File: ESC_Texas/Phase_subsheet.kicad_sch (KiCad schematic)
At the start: 14 parts, among them IC3 AD8411AWBRZ, IC4 MC78L05ACHT1G, J5 Conn_01x03_Pin, J6 Conn_01x03_Pin

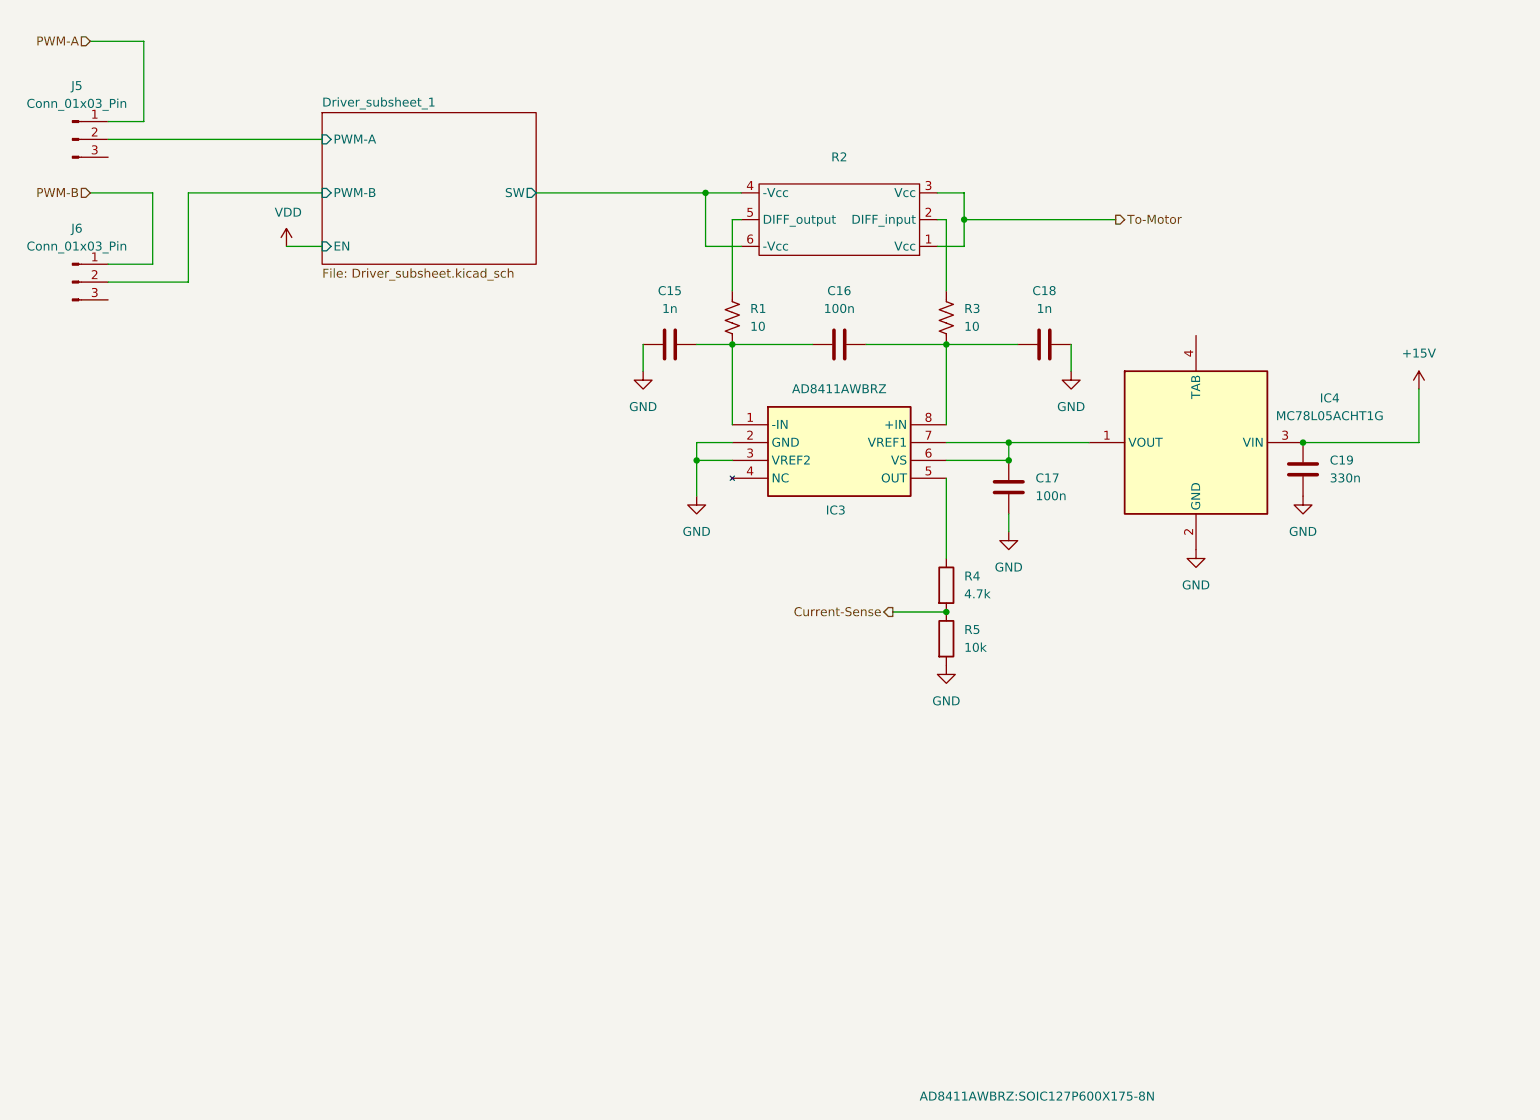
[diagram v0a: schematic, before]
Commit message: Added bypass capacitors to dc/dc...
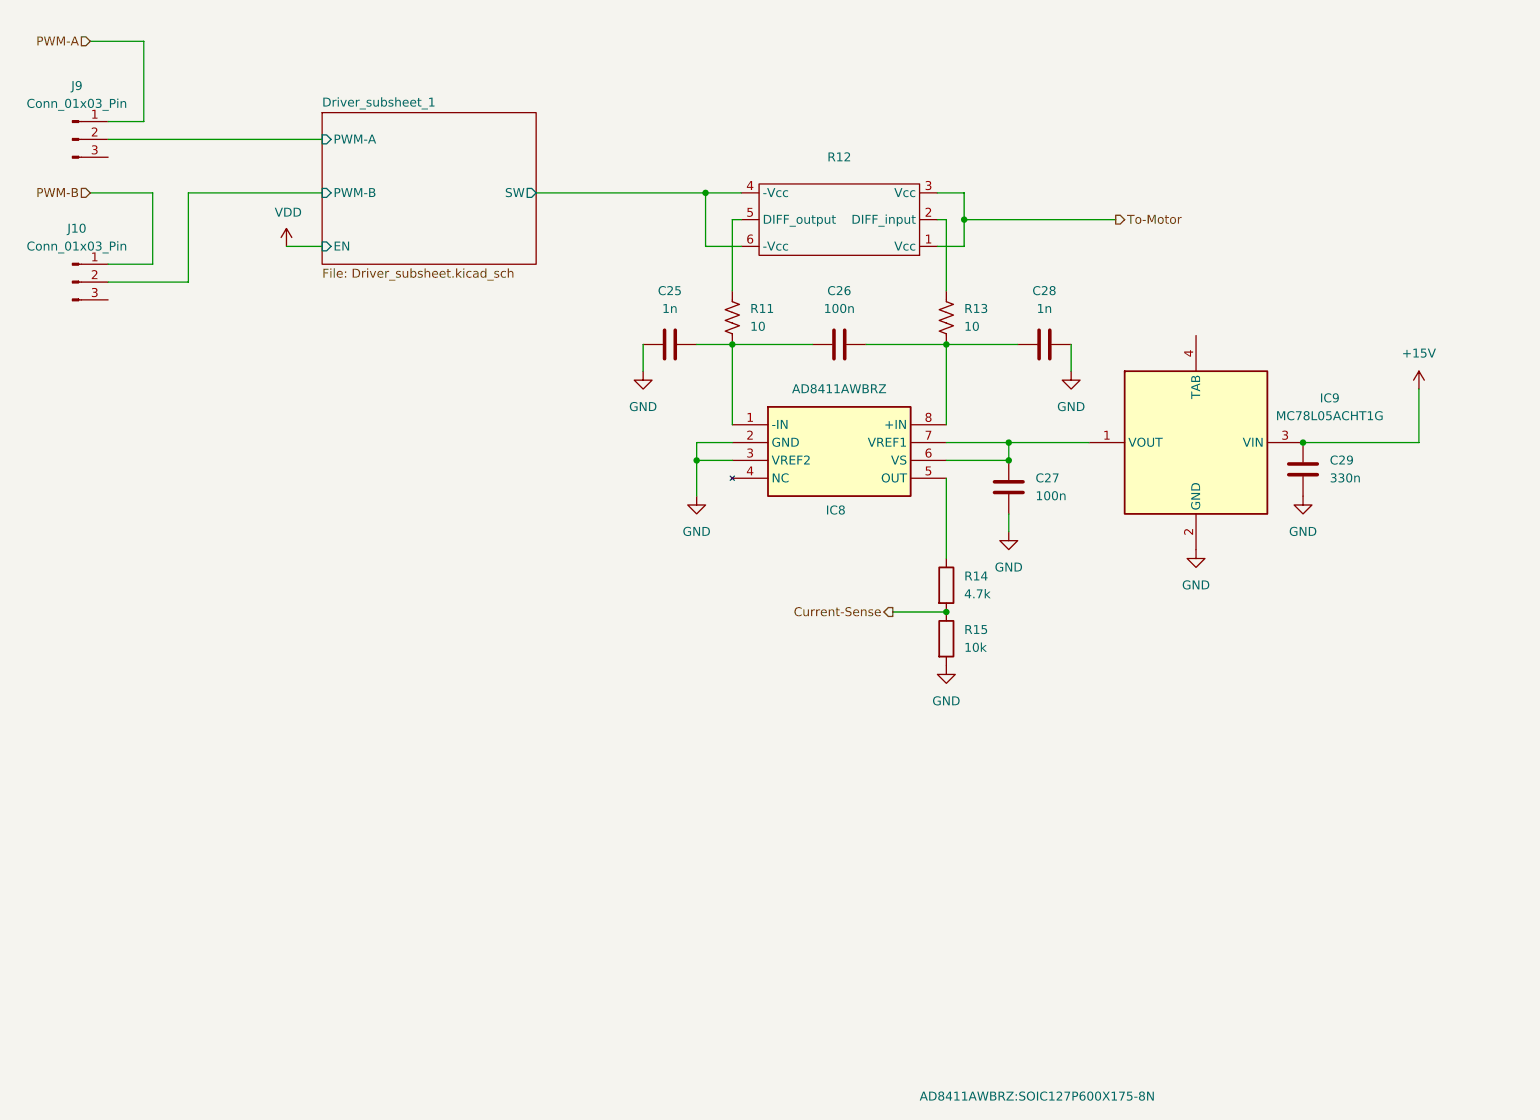
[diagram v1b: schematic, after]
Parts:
- renumbered C15 to C25, C16 to C26, C17 to C27, C18 to C28, C19 to C29, IC3 to IC8, IC4 to IC9, J6 to J10, J5 to J9, R1 to R11, R2 to R12, R3 to R13, R4 to R14, R5 to R15
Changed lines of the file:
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@@
 		(dnp no)
 		(fields_autoplaced yes)
-		(property "Reference" "C15"
+		(property "Reference" "C25"
 			(at 143.51 88.9 90)
 			(effects
@@
 		(dnp no)
 		(fields_autoplaced yes)
-		(property "Reference" "J5"
+		(property "Reference" "J9"
 			(at 59.055 59.69 0)
 			(effects
@@
 		(dnp no)
 		(fields_autoplaced yes)
-		(property "Reference" "#PWR037"
+		(property "Reference" "#PWR065"
 			(at 233.68 124.46 0)
 			(effects
@@
 		(dnp no)
 		(fields_autoplaced yes)
-		(property "Reference" "#PWR031"
+		(property "Reference" "#PWR059"
 			(at 139.7 106.68 0)
 			(effects
@@
 		(dnp no)
 		(fields_autoplaced yes)
-		(property "Reference" "C19"
+		(property "Reference" "C29"
 			(at 237.49 113.0299 0)
 			(effects
@@
 		(dnp no)
 		(fields_autoplaced yes)
-		(property "Reference" "#PWR034"
+		(property "Reference" "#PWR062"
 			(at 191.77 129.54 0)
 			(effects
@@
 		(dnp no)
 		(fields_autoplaced yes)
-		(property "Reference" "C17"
+		(property "Reference" "C27"
 			(at 195.58 115.5699 0)
 			(effects
@@
 		(dnp no)
 		(fields_autoplaced yes)
-		(property "Reference" "J6"
+		(property "Reference" "J10"
 			(at 59.055 80.01 0)
 			(effects
@@
 		(dnp no)
 		(fields_autoplaced yes)
-		(property "Reference" "R4"
+		(property "Reference" "R14"
 			(at 185.42 129.5399 0)
 			(effects
@@
 		(dnp no)
 		(fields_autoplaced yes)
-		(property "Reference" "#PWR033"
+		(property "Reference" "#PWR061"
 			(at 182.88 148.59 0)
 			(effects
@@
 		(on_board yes)
 		(dnp no)
-		(property "Reference" "#PWR030"
+		(property "Reference" "#PWR058"
 			(at 88.9 86.36 0)
 			(effects
@@
 		(dnp no)
 		(fields_autoplaced yes)
-		(property "Reference" "R1"
+		(property "Reference" "R11"
 			(at 154.94 91.4399 0)
 			(effects
@@
 		(dnp no)
 		(fields_autoplaced yes)
-		(property "Reference" "C18"
+		(property "Reference" "C28"
 			(at 196.85 88.9 90)
 			(effects
@@
 		(dnp no)
 		(fields_autoplaced yes)
-		(property "Reference" "C16"
+		(property "Reference" "C26"
 			(at 167.64 88.9 90)
 			(effects
@@
 		(dnp no)
 		(fields_autoplaced yes)
-		(property "Reference" "R2"
+		(property "Reference" "R12"
 			(at 167.64 69.85 0)
 			(effects
@@
 		(dnp no)
 		(fields_autoplaced yes)
-		(property "Reference" "#PWR032"
+		(property "Reference" "#PWR060"
 			(at 147.32 124.46 0)
 			(effects
@@
 		(on_board yes)
 		(dnp no)
-		(property "Reference" "IC3"
+		(property "Reference" "IC8"
 			(at 167.132 120.142 0)
 			(effects
@@
 		(dnp no)
 		(fields_autoplaced yes)
-		(property "Reference" "IC4"
+		(property "Reference" "IC9"
 			(at 237.49 104.1714 0)
 			(effects
@@
 		(dnp no)
 		(fields_autoplaced yes)
-		(property "Reference" "#PWR035"
+		(property "Reference" "#PWR063"
 			(at 200.66 106.68 0)
 			(effects
@@
 		(dnp no)
 		(fields_autoplaced yes)
-		(property "Reference" "#PWR036"
+		(property "Reference" "#PWR064"
 			(at 218.44 132.08 0)
 			(effects
@@
 		(dnp no)
 		(fields_autoplaced yes)
-		(property "Reference" "R5"
+		(property "Reference" "R15"
 			(at 185.42 137.1599 0)
 			(effects
@@
 		(dnp no)
 		(fields_autoplaced yes)
-		(property "Reference" "R3"
+		(property "Reference" "R13"
 			(at 185.42 91.4399 0)
 			(effects
@@
 		(dnp no)
 		(fields_autoplaced yes)
-		(property "Reference" "#PWR038"
+		(property "Reference" "#PWR066"
 			(at 250.19 106.68 0)
 			(effects

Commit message: PCB layout done
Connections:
- net GND: now also IC9.4 (TAB)
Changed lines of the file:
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@@
+	(wire
+		(pts
+			(xy 218.44 91.44) (xy 218.44 95.25)
+		)
+		(stroke
+			(width 0)
+			(type default)
+		)
+	)
 	(wire
 		(pts
@@
 	(wire
 		(pts
+			(xy 224.79 92.71) (xy 224.79 91.44)
+		)
+		(stroke
+			(width 0)
+			(type default)
+		)
+	)
+	(wire
+		(pts
 			(xy 191.77 120.65) (xy 191.77 123.19)
 		)
@@
 		(pts
 			(xy 152.4 88.9) (xy 152.4 78.74)
+		)
+		(stroke
+			(width 0)
+			(type default)
+		)
+	)
+	(wire
+		(pts
+			(xy 224.79 91.44) (xy 218.44 91.44)
 		)
 		(stroke
@@
 					(unit 1)
 				)
+			)
+		)
+	)
+	(symbol
+		(lib_id "power:GND")
+		(at 224.79 92.71 0)
+		(unit 1)
+		(exclude_from_sim no)
+		(in_bom yes)
+		(on_board yes)
+		(dnp no)
+		(fields_autoplaced yes)
+		(property "Reference" "#PWR085"
+			(at 224.79 99.06 0)
+			(effects
+				(font
+					(size 1.27 1.27)
+				)
+				(hide yes)
+			)
+		)
+		(property "Value" "GND"
+			(at 224.79 97.79 0)
+			(effects
+				(font
+					(size 1.27 1.27)
+				)
+			)
+		)
+		(property "Footprint" ""
+			(at 224.79 92.71 0)
+			(effects
+				(font
+					(size 1.27 1.27)
+				)
+				(hide yes)
+			)
+		)
+		(property "Datasheet" ""
+			(at 224.79 92.71 0)
+			(effects
+				(font
+					(size 1.27 1.27)
+				)
+				(hide yes)
+			)
+		)
+		(property "Description" "Power symbol creates a global label with name \"GND\" , ground"
+			(at 224.79 92.71 0)
+			(effects
+				(font
+					(size 1.27 1.27)
+				)
+				(hide yes)
+			)
+		)
+		(pin "1"
+		)
+		(instances
+			(project ""
+				(path "/0e3a5351-d2cd-4ecc-a1be-cca9c5f62ea0/553690e4-0a20-4b8e-821c-55ba3788d3c5"
+					(reference "#PWR086")
+					(unit 1)
+				)
+				(path "/0e3a5351-d2cd-4ecc-a1be-cca9c5f62ea0/63c8dce8-451d-41ee-b438-d688cf3e64bd"
+					(reference "#PWR085")
+					(unit 1)
+				)
+				(path "/0e3a5351-d2cd-4ecc-a1be-cca9c5f62ea0/b8e552f6-93a8-4098-a907-a65be165d984"
+					(reference "#PWR080")
+					(unit 1)
+				)

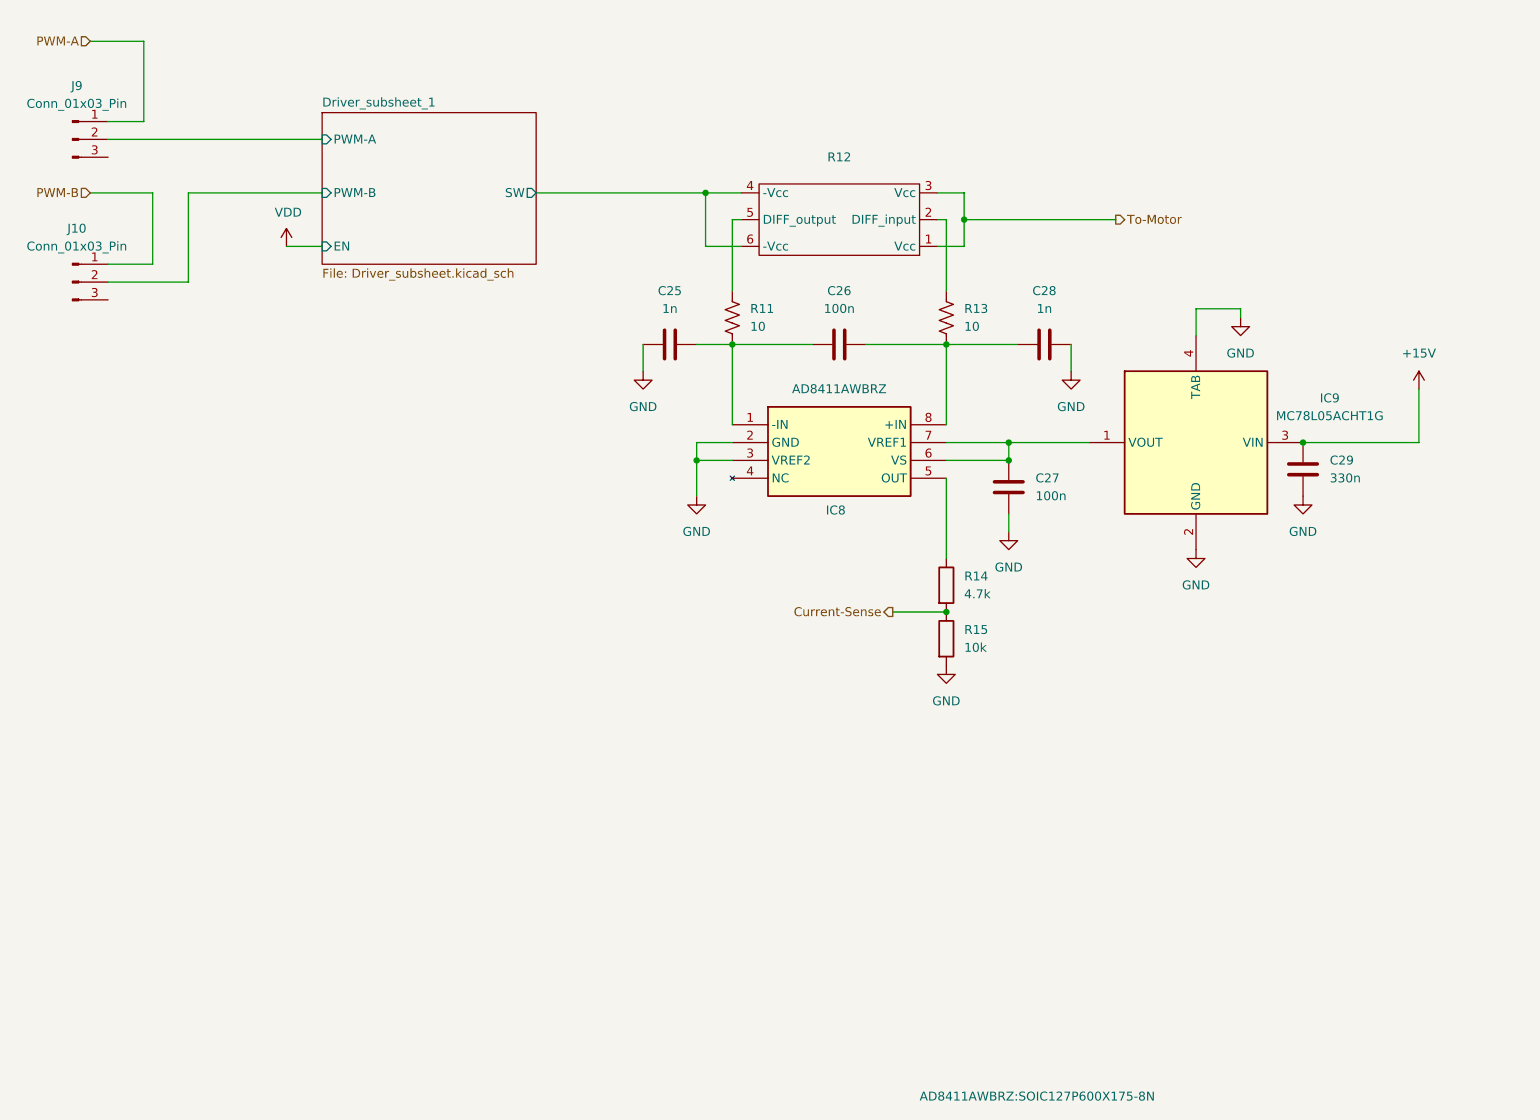
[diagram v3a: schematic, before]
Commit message: Started adding CAN Module
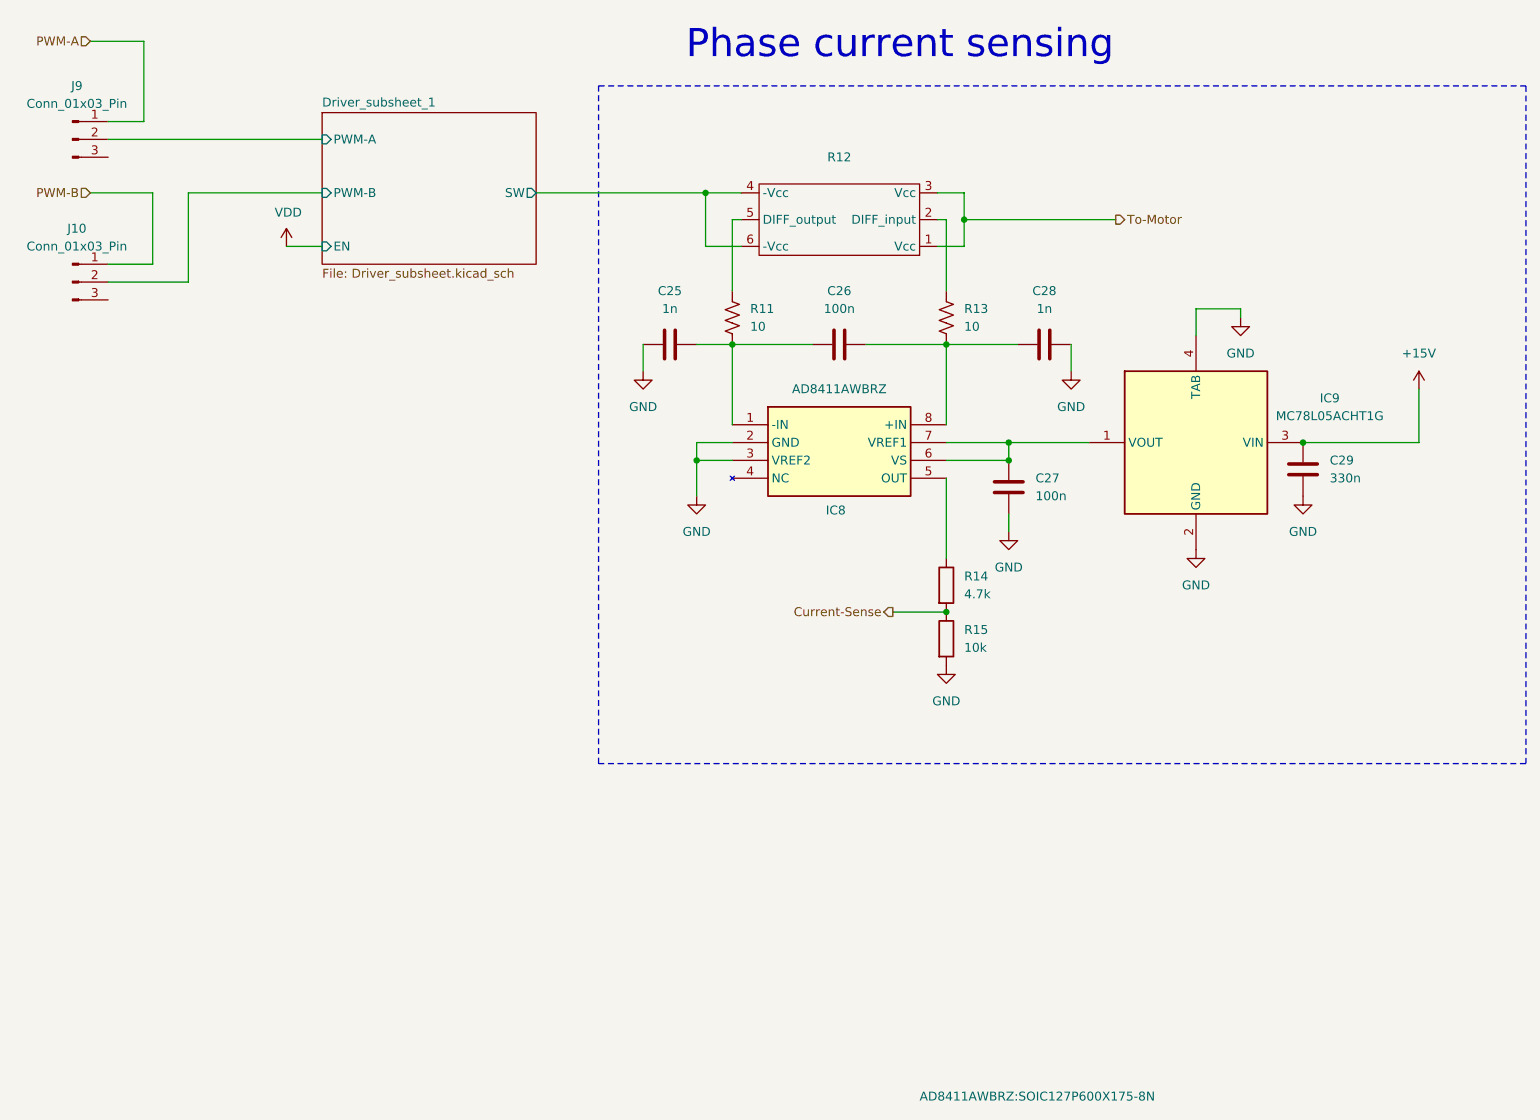
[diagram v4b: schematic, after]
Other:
- note added: "Phase current sensing"
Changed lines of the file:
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@@
+		)
+	)
+	(rectangle
+		(start 133.35 59.69)
+		(end 265.43 156.21)
+		(stroke
+			(width 0)
+			(type dash)
+		)
+		(fill
+			(type none)
+		)
+	)
+	(text "Phase current sensing"
+		(exclude_from_sim no)
+		(at 176.276 53.848 0)
+		(effects
+			(font
+				(size 4 4)
+			)
 		)
 	)
